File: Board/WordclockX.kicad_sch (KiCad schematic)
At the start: 129 parts, among them J1 USB_C_Receptacle_USB2.0, SW1 SW_Push_Dual, SW2 SW_Push_Dual, U1 W25Q16JLSNIG, U2 MCP7940N-xST, U3 RP2040, U4 MIC5504-3.3YM5, U5 74HCT137, U6 PCA9626, U7 PCA9626, Y1 12M, Y2 32768

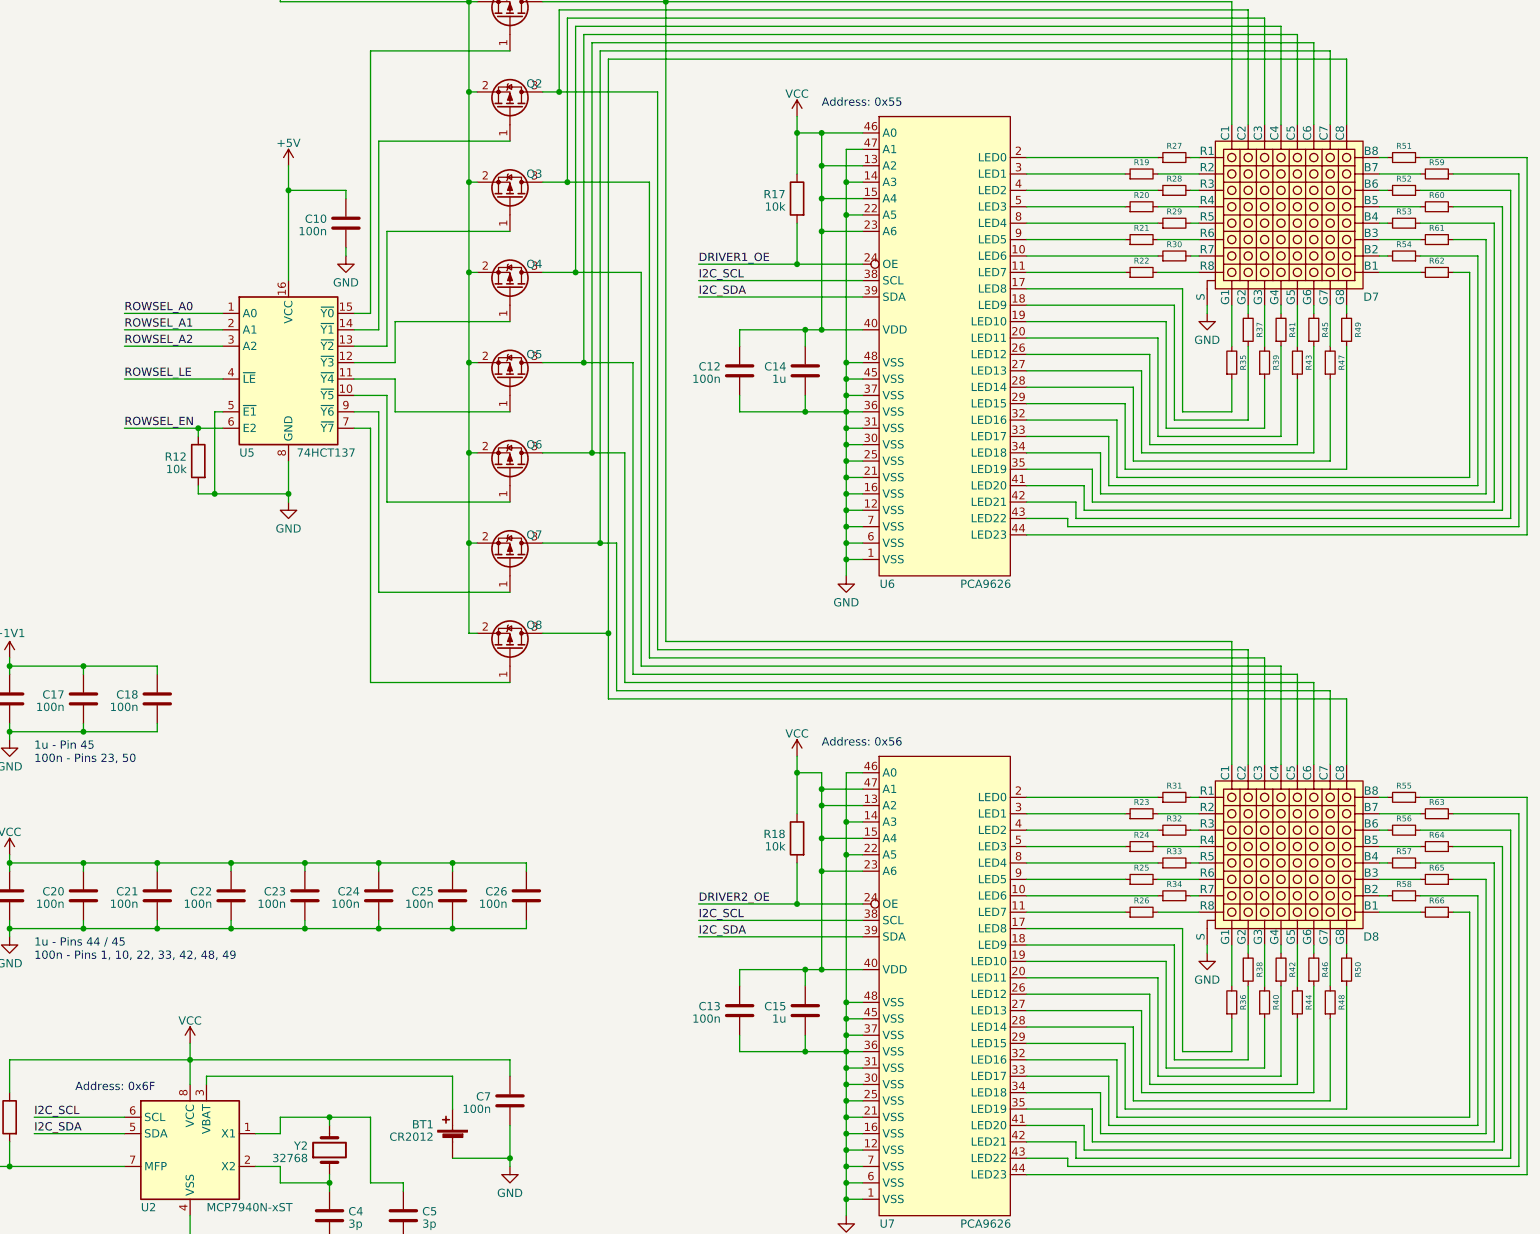
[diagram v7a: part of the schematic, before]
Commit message: Replaced individual resistors with resistor arrays
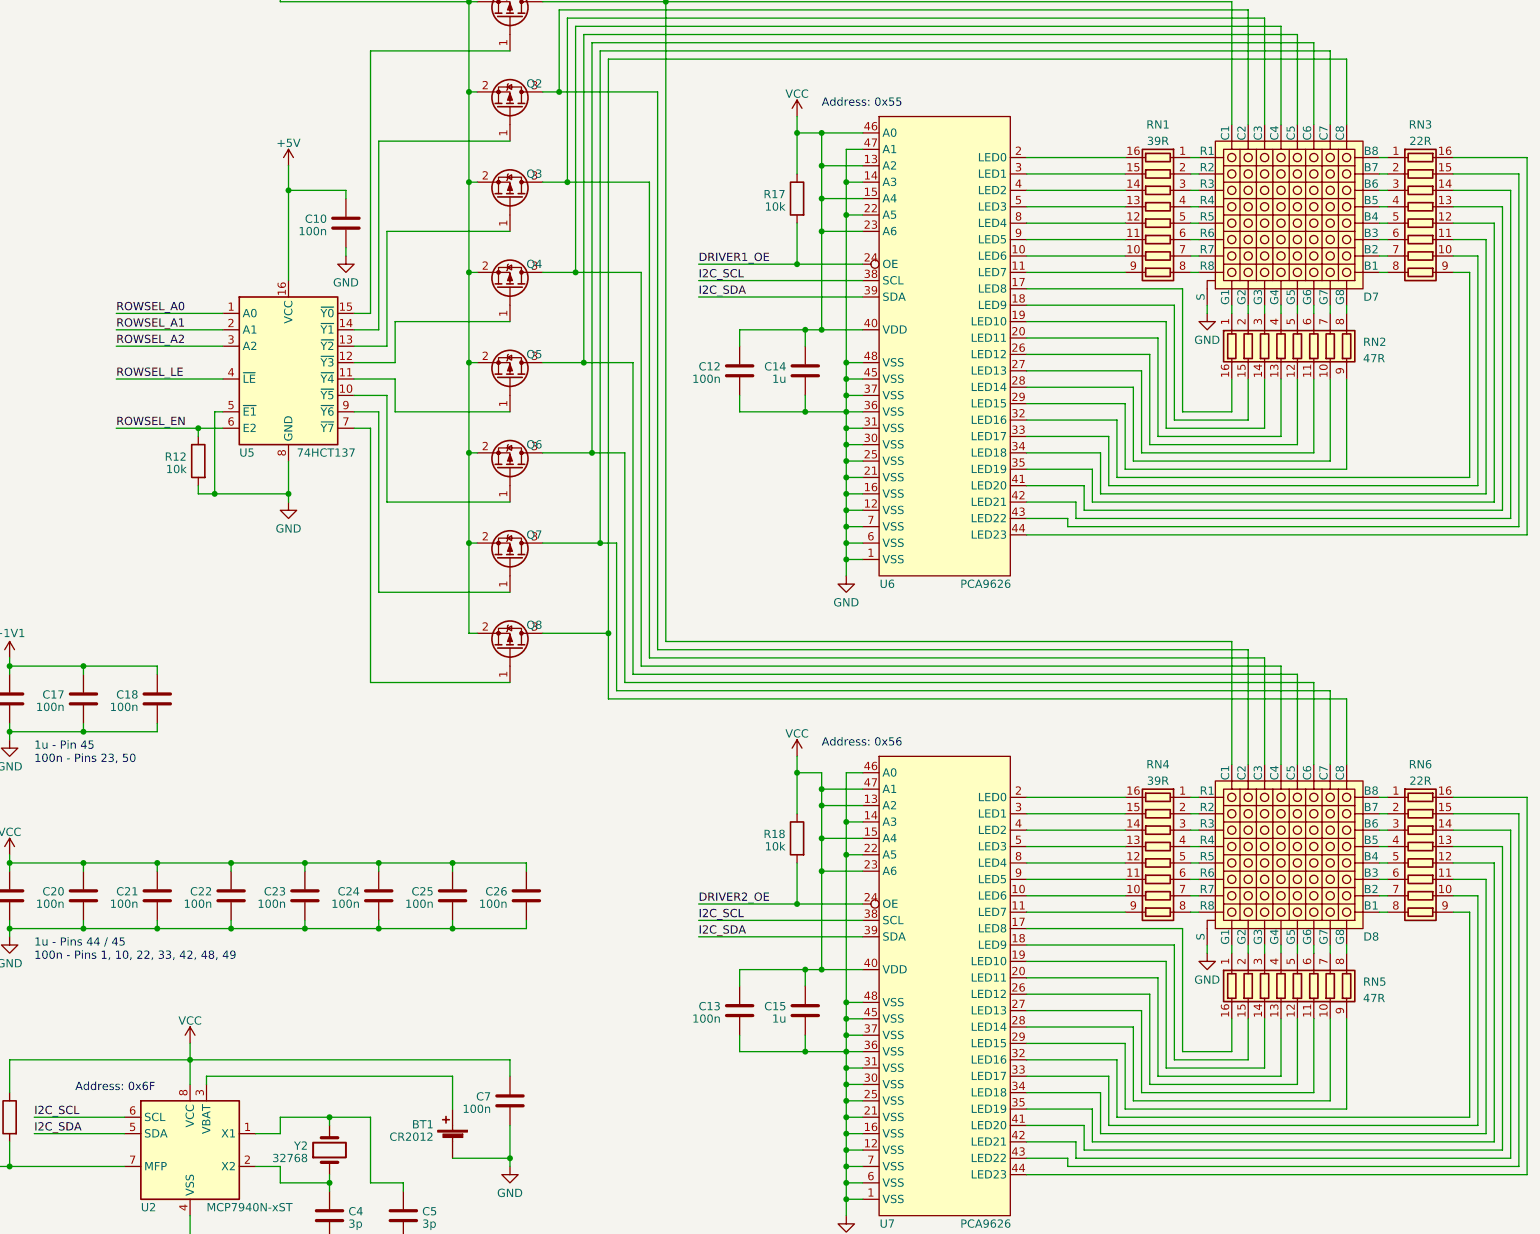
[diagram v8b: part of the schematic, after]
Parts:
- removed R19, R20, R21, R22, R23, R24, R25, R26, R27, R28, R29, R30, R31, R32, R33, R34, R35, R36, R37, R38, R39, R40, R41, R42, R43, R44, R45, R46, R47, R48, R49, R50, R51, R52, R53, R54, R55, R56, R57, R58, R59, R60, R61, R62, R63, R64, R65, R66: ~, Resistor_SMD:R_0603_1608Metric, symbol Device:R_Small
- added RN1, RN4: 39R, symbol Device:R_Pack08
- added RN2, RN5: 47R, symbol Device:R_Pack08
- added RN3, RN6: 22R, symbol Device:R_Pack08
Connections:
- net at U6.20 (LED11): now also RN2.13 (R4.2)
- net at D7.25 (G4): now also RN2.4 (R4.1)
- net at U7.34 (LED18): now also RN6.11 (R6.2)
- net at D8.3 (B3): now also RN6.6 (R6.1)
- net at U6.9 (LED5): now also RN1.11 (R6.2)
- net at D7.14 (R6): now also RN1.6 (R6.1)
- net at U6.29 (LED15): now also RN2.9 (R8.2)
- net at D7.21 (G8): now also RN2.8 (R8.1)
- net at U6.19 (LED10): now also RN2.14 (R3.2)
- net at D7.26 (G3): now also RN2.3 (R3.1)
- net at U6.3 (LED1): now also RN1.15 (R2.2)
- net at D7.10 (R2): now also RN1.2 (R2.1)
- net at U6.4 (LED2): now also RN1.14 (R3.2)
- net at D7.11 (R3): now also RN1.3 (R3.1)
- net at U6.26 (LED12): now also RN2.12 (R5.2)
- net at D7.24 (G5): now also RN2.5 (R5.1)
- net at U6.32 (LED16): now also RN3.9 (R8.2)
- net at D7.1 (B1): now also RN3.8 (R8.1)
- net at U7.10 (LED6): now also RN4.10 (R7.2)
- net at U7.11 (LED7): now also RN4.9 (R8.2)
- net at U7.17 (LED8): now also RN5.16 (R1.2)
- net at U7.18 (LED9): now also RN5.15 (R2.2)
- net at U7.19 (LED10): now also RN5.14 (R3.2)
- net at U7.2 (LED0): now also RN4.16 (R1.2)
- net at U7.20 (LED11): now also RN5.13 (R4.2)
- net at U7.26 (LED12): now also RN5.12 (R5.2)
- net at U7.27 (LED13): now also RN5.11 (R6.2)
- net at U7.28 (LED14): now also RN5.10 (R7.2)
- net at U7.29 (LED15): now also RN5.9 (R8.2)
- net at U7.3 (LED1): now also RN4.15 (R2.2)
- net at U7.32 (LED16): now also RN6.9 (R8.2)
- net at U7.33 (LED17): now also RN6.10 (R7.2)
- net at U7.35 (LED19): now also RN6.12 (R5.2)
- net at U7.4 (LED2): now also RN4.14 (R3.2)
- net at U7.41 (LED20): now also RN6.13 (R4.2)
- net at U7.42 (LED21): now also RN6.14 (R3.2)
- net at U7.43 (LED22): now also RN6.15 (R2.2)
- net at U7.44 (LED23): now also RN6.16 (R1.2)
- net at U7.5 (LED3): now also RN4.13 (R4.2)
- net at U7.8 (LED4): now also RN4.12 (R5.2)
- net at U7.9 (LED5): now also RN4.11 (R6.2)
- net at U6.18 (LED9): now also RN2.15 (R2.2)
- net at D7.27 (G2): now also RN2.2 (R2.1)
- net at D8.14 (R6): now also RN4.6 (R6.1)
- net at D8.7 (B7): now also RN6.2 (R2.1)
- net at D7.12 (R4): now also RN1.4 (R4.1)
- net at D7.13 (R5): now also RN1.5 (R5.1)
- net at D7.15 (R7): now also RN1.7 (R7.1)
- net at D7.16 (R8): now also RN1.8 (R8.1)
- net at D7.2 (B2): now also RN3.7 (R7.1)
- net at D7.22 (G7): now also RN2.7 (R7.1)
- net at D7.23 (G6): now also RN2.6 (R6.1)
- net at D7.28 (G1): now also RN2.1 (R1.1)
- net at D7.3 (B3): now also RN3.6 (R6.1)
- net at D7.4 (B4): now also RN3.5 (R5.1)
- net at D7.5 (B5): now also RN3.4 (R4.1)
- net at D7.6 (B6): now also RN3.3 (R3.1)
- net at D7.7 (B7): now also RN3.2 (R2.1)
- net at D7.8 (B8): now also RN3.1 (R1.1)
- net at D7.9 (R1): now also RN1.1 (R1.1)
- net at D8.1 (B1): now also RN6.8 (R8.1)
- net at D8.10 (R2): now also RN4.2 (R2.1)
- net at D8.11 (R3): now also RN4.3 (R3.1)
- net at D8.12 (R4): now also RN4.4 (R4.1)
- net at D8.13 (R5): now also RN4.5 (R5.1)
- net at D8.15 (R7): now also RN4.7 (R7.1)
- net at D8.16 (R8): now also RN4.8 (R8.1)
- net at D8.2 (B2): now also RN6.7 (R7.1)
- net at D8.21 (G8): now also RN5.8 (R8.1)
- net at D8.22 (G7): now also RN5.7 (R7.1)
- net at D8.23 (G6): now also RN5.6 (R6.1)
- net at D8.24 (G5): now also RN5.5 (R5.1)
- net at D8.25 (G4): now also RN5.4 (R4.1)
- net at D8.26 (G3): now also RN5.3 (R3.1)
- net at D8.27 (G2): now also RN5.2 (R2.1)
- net at D8.28 (G1): now also RN5.1 (R1.1)
- net at D8.4 (B4): now also RN6.5 (R5.1)
- net at D8.5 (B5): now also RN6.4 (R4.1)
- net at D8.6 (B6): now also RN6.3 (R3.1)
- net at D8.8 (B8): now also RN6.1 (R1.1)
- net at D8.9 (R1): now also RN4.1 (R1.1)
- net at U6.17 (LED8): now also RN2.16 (R1.2)
- net at U6.8 (LED4): now also RN1.12 (R5.2)
- net at U6.33 (LED17): now also RN3.10 (R7.2)
- net at U6.28 (LED14): now also RN2.10 (R7.2)
- net at U6.10 (LED6): now also RN1.10 (R7.2)
- net at U6.11 (LED7): now also RN1.9 (R8.2)
- net at U6.2 (LED0): now also RN1.16 (R1.2)
- net at U6.27 (LED13): now also RN2.11 (R6.2)
- net at U6.34 (LED18): now also RN3.11 (R6.2)
- net at U6.35 (LED19): now also RN3.12 (R5.2)
- net at U6.41 (LED20): now also RN3.13 (R4.2)
- net at U6.42 (LED21): now also RN3.14 (R3.2)
- net at U6.43 (LED22): now also RN3.15 (R2.2)
- net at U6.44 (LED23): now also RN3.16 (R1.2)
- net at U6.5 (LED3): now also RN1.13 (R4.2)
